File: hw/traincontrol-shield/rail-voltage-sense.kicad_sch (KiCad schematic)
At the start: 0 parts

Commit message: Phase 3+4 complete: implement all 8 schematics, fix KiCad 9 lib embedding
All 7 sub-sheets and top-level sheet fully implemented and validated with
kicad-cli (exit 0 on all 8 files).

Key fixes to lib_sym_entry() in generator scripts:
- Sub-symbol names must NOT include library prefix (KiCad 9 parser requirement)
- Local KiCad 6 library symbols upgraded inline: remove (id N) from properties,
  strip stroke colors, fix bare 'hide', add exclude_from_sim + embedded_fonts
- Derived symbols (MOC3021M extends MOC3010M) flattened by copying base
  graphics into derived, removing (extends ...) for standalone embedding

Validated: kicad-cli sch export netlist exits 0 for all 8 .kicad_sch files.

Co-Authored-By: Claude Sonnet 4.6 <noreply@anthropic.com>
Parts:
- added R10: 27kΩ, Resistor_SMD:R_0603_1608Metric, symbol Device:R
- added R9: 100kΩ, Resistor_SMD:R_0603_1608Metric, symbol Device:R
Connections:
- new net +15V: R9.1
- new net GND: R10.2
- new net VSENSE: R10.1, R9.2
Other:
- title: Traincontrol Shield — Rail Voltage Sense -> Rail Voltage Sense
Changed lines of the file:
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@@
 	(paper "A4")
 	(title_block
-		(title "Traincontrol Shield — Rail Voltage Sense")
+		(title "Rail Voltage Sense")
 		(date "2026-02-21")
 		(rev "1")
 		(company "")
 	)
-	(sheet_instances
-		(path "/"
-			(page "1")
+	(symbol
+		(lib_id "Device:R")
+		(at 80.01 80.01 0)
+		(unit 1)
+		(exclude_from_sim no)
+		(in_bom yes)
+		(on_board yes)
+		(dnp no)
+		(property "Reference" "R9"
+			(at 80.01 76.01 0)
+			(effects (font (size 1.27 1.27)))
+		)
+		(property "Value" "100kΩ"
+			(at 80.01 84.01 0)
+			(effects (font (size 1.27 1.27)))
+		)
+		(property "Footprint" "Resistor_SMD:R_0603_1608Metric"
+			(at 80.01 80.01 0)
+			(effects (font (size 1.27 1.27)) (hide yes))
+		)
+		(property "Datasheet" "~"
+			(at 80.01 80.01 0)
+			(effects (font (size 1.27 1.27)) (hide yes))
+		)
+		(pin "1")
+		(pin "2")
+		(instances
+			(project "traincontrol-shield"
+				(path "/12cc2a67-9b1c-41e4-828f-9c2a8df6bb35/a8cf3e0f-6d5f-4a60-9682-8cd8e6228106"
+					(reference "R9")
+					(unit 1)
+				)
+			)
 		)
 	)
+	(symbol
+		(lib_id "Device:R")
+		(at 80.01 87.63 0)
+		(unit 1)
+		(exclude_from_sim no)
+		(in_bom yes)
+		(on_board yes)
+		(dnp no)
+		(property "Reference" "R10"
+			(at 80.01 83.63 0)
+			(effects (font (size 1.27 1.27)))
+		)
+		(property "Value" "27kΩ"
+			(at 80.01 91.63 0)
+			(effects (font (size 1.27 1.27)))
+		)
+		(property "Footprint" "Resistor_SMD:R_0603_1608Metric"
+			(at 80.01 87.63 0)
+			(effects (font (size 1.27 1.27)) (hide yes))
+		)
+		(property "Datasheet" "~"
+			(at 80.01 87.63 0)
+			(effects (font (size 1.27 1.27)) (hide yes))
+		)
+		(pin "1")
+		(pin "2")
+		(instances
+			(project "traincontrol-shield"
+				(path "/12cc2a67-9b1c-41e4-828f-9c2a8df6bb35/a8cf3e0f-6d5f-4a60-9682-8cd8e6228106"
+					(reference "R10")
+					(unit 1)
+				)
+			)
+		)
+	)
+	(symbol
+		(lib_id "power:+15V")
+		(at 80.01 76.2 0)
+		(unit 1)
+		(exclude_from_sim yes)
+		(in_bom no)
+		(on_board yes)
+		(dnp no)
+		(property "Reference" "#PWR01"
+			(at 80.01 74.2 0)
+			(effects (font (size 1.27 1.27)) (hide yes))
+		)
+		(property "Value" "+15V"
+			(at 80.01 78.2 0)
+			(effects (font (size 1.27 1.27)))
+		)
+		(property "Footprint" ""
+			(at 80.01 76.2 0)
+			(effects (font (size 1.27 1.27)) (hide yes))
+		)
+		(property "Datasheet" ""
+			(at 80.01 76.2 0)
+			(effects (font (size 1.27 1.27)) (hide yes))
+		)
+		(pin "1")
+		(instances
+			(project "traincontrol-shield"
+				(path "/12cc2a67-9b1c-41e4-828f-9c2a8df6bb35/a8cf3e0f-6d5f-4a60-9682-8cd8e6228106"
+					(reference "#PWR01")
+					(unit 1)
+				)
+			)
+		)
+	)
+	(symbol
+		(lib_id "power:GND")
+		(at 80.01 91.44 0)
+		(unit 1)
+		(exclude_from_sim yes)
+		(in_bom no)
+		(on_board yes)
+		(dnp no)
+		(property "Reference" "#PWR02"
+			(at 80.01 89.44 0)
+			(effects (font (size 1.27 1.27)) (hide yes))
+		)
+		(property "Value" "GND"
+			(at 80.01 93.44 0)
+			(effects (font (size 1.27 1.27)))
+		)
+		(property "Footprint" ""
+			(at 80.01 91.44 0)
+			(effects (font (size 1.27 1.27)) (hide yes))
+		)
+		(property "Datasheet" ""
+			(at 80.01 91.44 0)
+			(effects (font (size 1.27 1.27)) (hide yes))
+		)
+		(pin "1")
+		(instances
+			(project "traincontrol-shield"
+				(path "/12cc2a67-9b1c-41e4-828f-9c2a8df6bb35/a8cf3e0f-6d5f-4a60-9682-8cd8e6228106"
+					(reference "#PWR02")
+					(unit 1)
+				)
+			)
+		)
+	)
+	(junction
+		(at 80.01 83.82)
+		(diameter 0)
+		(color 0 0 0 0)
+	)
+	(global_label "VSENSE"
+		(shape output)
+		(at 92.71 83.82 0)
+		(fields_autoplaced yes)
+		(effects (font (size 1.27 1.27)) (justify left bottom))
+		(property "Intersheetrefs" "${INTERSHEET_REFS}"
+			(at 92.71 83.82 0)
+			(effects (font (size 1.27 1.27)) (hide yes))
+		)
+	)
+	(wire
+		(pts (xy 80.01 83.82) (xy 92.71 83.82))
+		(stroke (width 0) (type solid))
+	)
+	(sheet_instances
+		(path "/12cc2a67-9b1c-41e4-828f-9c2a8df6bb35/a8cf3e0f-6d5f-4a60-9682-8cd8e6228106"
+			(page "7")
+		)
+	)

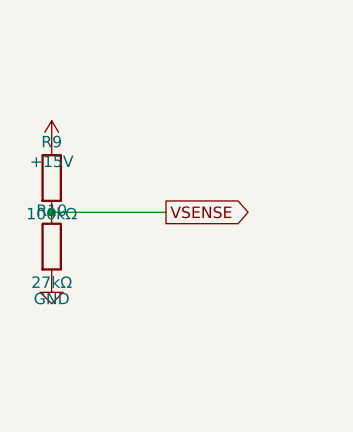
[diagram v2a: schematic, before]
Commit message: Add 2.54mm wire stubs to all power and global label connections
Power symbols (GND/+V) and global labels were placed directly on
component pins, making connections invisible in KiCad GUI. Add a
2.54mm stub wire between each component pin and power symbol/label
so connections are visually distinct. GND stubs go down (+y), +V
stubs go up (-y), label stubs go horizontally away from pin.
PWR_FLAG symbols are excluded (already have explicit wires).

All 8 schematics validate with kicad-cli exit 0.

Co-Authored-By: Claude Sonnet 4.6 <noreply@anthropic.com>
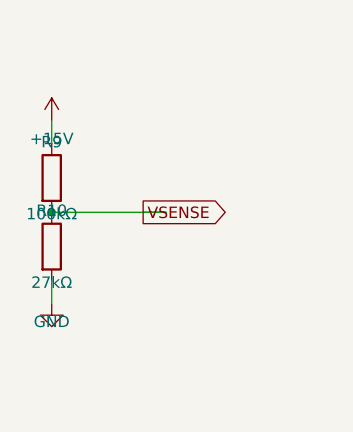
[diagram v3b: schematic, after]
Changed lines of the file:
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@@
 		)
+	)
+	(wire
+		(pts (xy 80.01 76.2) (xy 80.01 73.66))
+		(stroke (width 0) (type solid))
 	)
 	(symbol
 		(lib_id "power:+15V")
-		(at 80.01 76.2 0)
+		(at 80.01 73.66 0)
 		(unit 1)
 		(exclude_from_sim no)
@@
 		(dnp no)
 		(property "Reference" "#PWR01"
-			(at 80.01 74.2 0)
+			(at 80.01 71.66 0)
 			(effects (font (size 1.27 1.27)) (hide yes))
 		)
 		(property "Value" "+15V"
-			(at 80.01 78.2 0)
+			(at 80.01 75.66 0)
 			(effects (font (size 1.27 1.27)))
 		)
 		(property "Footprint" ""
-			(at 80.01 76.2 0)
+			(at 80.01 73.66 0)
 			(effects (font (size 1.27 1.27)) (hide yes))
 		)
 		(property "Datasheet" ""
-			(at 80.01 76.2 0)
+			(at 80.01 73.66 0)
 			(effects (font (size 1.27 1.27)) (hide yes))
 		)
@@
 		)
 	)
+	(wire
+		(pts (xy 80.01 91.44) (xy 80.01 93.98))
+		(stroke (width 0) (type solid))
+	)
 	(symbol
 		(lib_id "power:GND")
-		(at 80.01 91.44 0)
+		(at 80.01 93.98 0)
 		(unit 1)
 		(exclude_from_sim no)
@@
 		(dnp no)
 		(property "Reference" "#PWR02"
-			(at 80.01 89.44 0)
+			(at 80.01 91.98 0)
 			(effects (font (size 1.27 1.27)) (hide yes))
 		)
 		(property "Value" "GND"
-			(at 80.01 93.44 0)
+			(at 80.01 95.98 0)
 			(effects (font (size 1.27 1.27)))
 		)
 		(property "Footprint" ""
-			(at 80.01 91.44 0)
+			(at 80.01 93.98 0)
 			(effects (font (size 1.27 1.27)) (hide yes))
 		)
 		(property "Datasheet" ""
-			(at 80.01 91.44 0)
+			(at 80.01 93.98 0)
 			(effects (font (size 1.27 1.27)) (hide yes))
 		)
@@
 		(color 0 0 0 0)
 	)
+	(wire
+		(pts (xy 90.16999999999999 83.82) (xy 92.71 83.82))
+		(stroke (width 0) (type solid))
+	)
 	(global_label "VSENSE"
 		(shape output)
-		(at 92.71 83.82 0)
+		(at 90.16999999999999 83.82 0)
 		(fields_autoplaced yes)
 		(effects (font (size 1.27 1.27)) (justify left bottom))
 		(property "Intersheetrefs" "${INTERSHEET_REFS}"
-			(at 92.71 83.82 0)
+			(at 90.16999999999999 83.82 0)
 			(effects (font (size 1.27 1.27)) (hide yes))
 		)

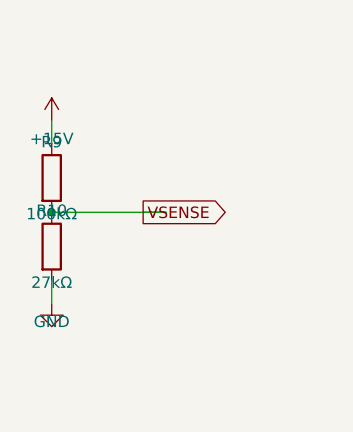
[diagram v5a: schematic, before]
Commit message: Add hierarchical ports to all sub-sheets and top-level connections
Replace inter-sheet global_label elements with hierarchical_label in all
sub-sheets, so each sheet exports visible ports on its sheet box symbol
in the top-level. Add matching (pin ...) entries to every sheet block in
the top-level. Connect all sheet pins with bidirectional global_labels in
the inter-column gap (x=105..120) so named nets auto-join.

Port counts per sub-sheet:
  power-supply:       2  (AC_IN, AC_RTN)
  zero-crossing:      3  (AC_IN, AC_RTN, ZC_OUT)
  xor-interlock:      6  (CTRL_A×2, CTRL_B×2, PHASE_A, PHASE_B)
  opto-triac-drive:   6  (PHASE_A, PHASE_B, AC_RTN×2, TRIAC_A_GATE, TRIAC_B_GATE)
  triacs-snubbers:   12  (AC_RTN×2, WINDING_A×3, WINDING_B×3, TRIAC_A_GATE, TRIAC_B_GATE)
  rail-voltage-sense: 1  (VSENSE)
  mcu:                4  (CTRL_A, CTRL_B, ZC_OUT, VSENSE)

All 8 schematics validate: kicad-cli exit 0.
Fix: correct KiCad 9 keyword is `hierarchical_label`, not `hier_label`.

Co-Authored-By: Claude Sonnet 4.6 <noreply@anthropic.com>
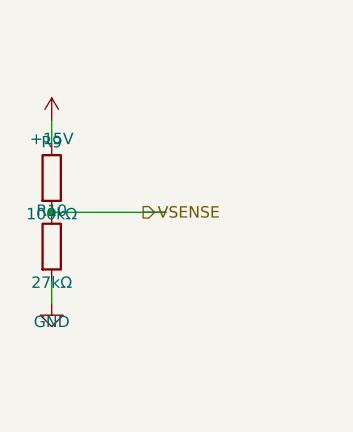
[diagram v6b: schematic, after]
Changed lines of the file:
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@@
 		(stroke (width 0) (type solid))
 	)
-	(global_label "VSENSE"
+	(hierarchical_label "VSENSE"
 		(shape output)
 		(at 90.16999999999999 83.82 0)

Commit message: Disperse component layout and triple wire stub length across all sheets
- STUB: 2.54 → 7.62 mm (3×) in all three generator scripts
- Inter-component spacing doubled in power-supply, MCU, and logic sheets
- Top-level inter-column gap widened (LX 120 → 130 mm) to avoid label collision
- Sheet frame heights made variable per pin count (20–35 mm)
- Right-column sheet x-origin and connector J4/J5/J6 x-positions updated accordingly
- All 8 sheets regenerated and validated with kicad-cli

Co-Authored-By: Claude Sonnet 4.6 <noreply@anthropic.com>
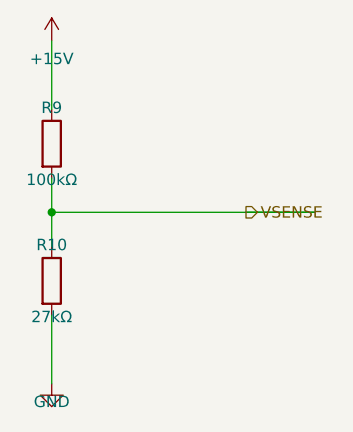
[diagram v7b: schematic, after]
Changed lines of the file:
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@@
 	(symbol
 		(lib_id "Device:R")
-		(at 80.01 80.01 0)
+		(at 80.01 76.2 0)
 		(unit 1)
 		(exclude_from_sim no)
@@
 		(dnp no)
 		(property "Reference" "R9"
-			(at 80.01 76.01 0)
+			(at 80.01 72.2 0)
 			(effects (font (size 1.27 1.27)))
 		)
 		(property "Value" "100kΩ"
-			(at 80.01 84.01 0)
+			(at 80.01 80.2 0)
 			(effects (font (size 1.27 1.27)))
 		)
 		(property "Footprint" "Resistor_SMD:R_0603_1608Metric"
-			(at 80.01 80.01 0)
+			(at 80.01 76.2 0)
 			(effects (font (size 1.27 1.27)) (hide yes))
 		)
 		(property "Datasheet" "~"
-			(at 80.01 80.01 0)
+			(at 80.01 76.2 0)
 			(effects (font (size 1.27 1.27)) (hide yes))
 		)
@@
 	(symbol
 		(lib_id "Device:R")
-		(at 80.01 87.63 0)
+		(at 80.01 91.44 0)
 		(unit 1)
 		(exclude_from_sim no)
@@
 		(dnp no)
 		(property "Reference" "R10"
-			(at 80.01 83.63 0)
+			(at 80.01 87.44 0)
 			(effects (font (size 1.27 1.27)))
 		)
 		(property "Value" "27kΩ"
-			(at 80.01 91.63 0)
+			(at 80.01 95.44 0)
 			(effects (font (size 1.27 1.27)))
 		)
 		(property "Footprint" "Resistor_SMD:R_0603_1608Metric"
-			(at 80.01 87.63 0)
+			(at 80.01 91.44 0)
 			(effects (font (size 1.27 1.27)) (hide yes))
 		)
 		(property "Datasheet" "~"
-			(at 80.01 87.63 0)
+			(at 80.01 91.44 0)
 			(effects (font (size 1.27 1.27)) (hide yes))
 		)
@@
 	)
 	(wire
-		(pts (xy 80.01 76.2) (xy 80.01 73.66))
+		(pts (xy 80.01 72.39) (xy 80.01 64.77))
 		(stroke (width 0) (type solid))
 	)
 	(symbol
 		(lib_id "power:+15V")
-		(at 80.01 73.66 0)
+		(at 80.01 64.77 0)
 		(unit 1)
 		(exclude_from_sim no)
@@
 		(dnp no)
 		(property "Reference" "#PWR01"
-			(at 80.01 71.66 0)
+			(at 80.01 62.769999999999996 0)
 			(effects (font (size 1.27 1.27)) (hide yes))
 		)
 		(property "Value" "+15V"
-			(at 80.01 75.66 0)
+			(at 80.01 66.77 0)
 			(effects (font (size 1.27 1.27)))
 		)
 		(property "Footprint" ""
-			(at 80.01 73.66 0)
+			(at 80.01 64.77 0)
 			(effects (font (size 1.27 1.27)) (hide yes))
 		)
 		(property "Datasheet" ""
-			(at 80.01 73.66 0)
+			(at 80.01 64.77 0)
 			(effects (font (size 1.27 1.27)) (hide yes))
 		)
@@
 	)
 	(wire
-		(pts (xy 80.01 91.44) (xy 80.01 93.98))
+		(pts (xy 80.01 95.25) (xy 80.01 102.87))
 		(stroke (width 0) (type solid))
 	)
 	(symbol
 		(lib_id "power:GND")
-		(at 80.01 93.98 0)
+		(at 80.01 102.87 0)
 		(unit 1)
 		(exclude_from_sim no)
@@
 		(dnp no)
 		(property "Reference" "#PWR02"
-			(at 80.01 91.98 0)
+			(at 80.01 100.87 0)
 			(effects (font (size 1.27 1.27)) (hide yes))
 		)
 		(property "Value" "GND"
-			(at 80.01 95.98 0)
+			(at 80.01 104.87 0)
 			(effects (font (size 1.27 1.27)))
 		)
 		(property "Footprint" ""
-			(at 80.01 93.98 0)
+			(at 80.01 102.87 0)
 			(effects (font (size 1.27 1.27)) (hide yes))
 		)
 		(property "Datasheet" ""
-			(at 80.01 93.98 0)
+			(at 80.01 102.87 0)
 			(effects (font (size 1.27 1.27)) (hide yes))
 		)
@@
 		)
 	)
+	(wire
+		(pts (xy 80.01 80.01) (xy 80.01 87.63))
+		(stroke (width 0) (type solid))
+	)
 	(junction
 		(at 80.01 83.82)
@@
 	)
 	(wire
-		(pts (xy 90.16999999999999 83.82) (xy 92.71 83.82))
+		(pts (xy 80.01 83.82) (xy 109.22 83.82))
+		(stroke (width 0) (type solid))
+	)
+	(wire
+		(pts (xy 101.6 83.82) (xy 109.22 83.82))
 		(stroke (width 0) (type solid))
 	)
 	(hierarchical_label "VSENSE"
 		(shape output)
-		(at 90.16999999999999 83.82 0)
+		(at 101.6 83.82 0)
 		(fields_autoplaced yes)
 		(effects (font (size 1.27 1.27)) (justify left bottom))
 		(property "Intersheetrefs" "${INTERSHEET_REFS}"
-			(at 90.16999999999999 83.82 0)
+			(at 101.6 83.82 0)
 			(effects (font (size 1.27 1.27)) (hide yes))
 		)
 	)
-	(wire
-		(pts (xy 80.01 83.82) (xy 92.71 83.82))
-		(stroke (width 0) (type solid))
-	)
 	(sheet_instances
